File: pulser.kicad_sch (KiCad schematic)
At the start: 15 parts, among them U3 MAX14808ETK_

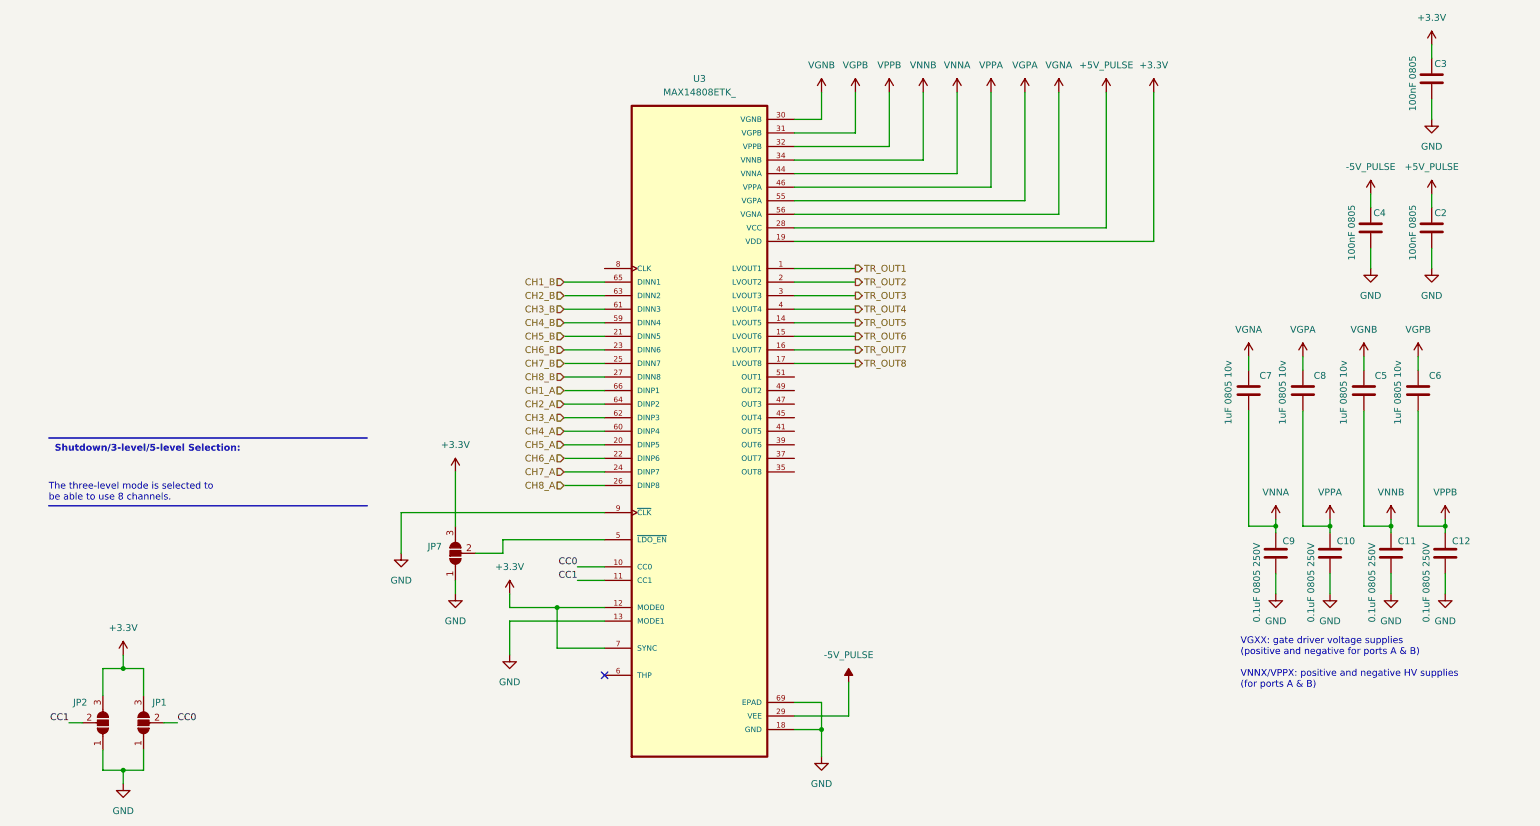
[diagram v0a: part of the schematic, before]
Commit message: finished pulser & mcu, receiver & power remaining
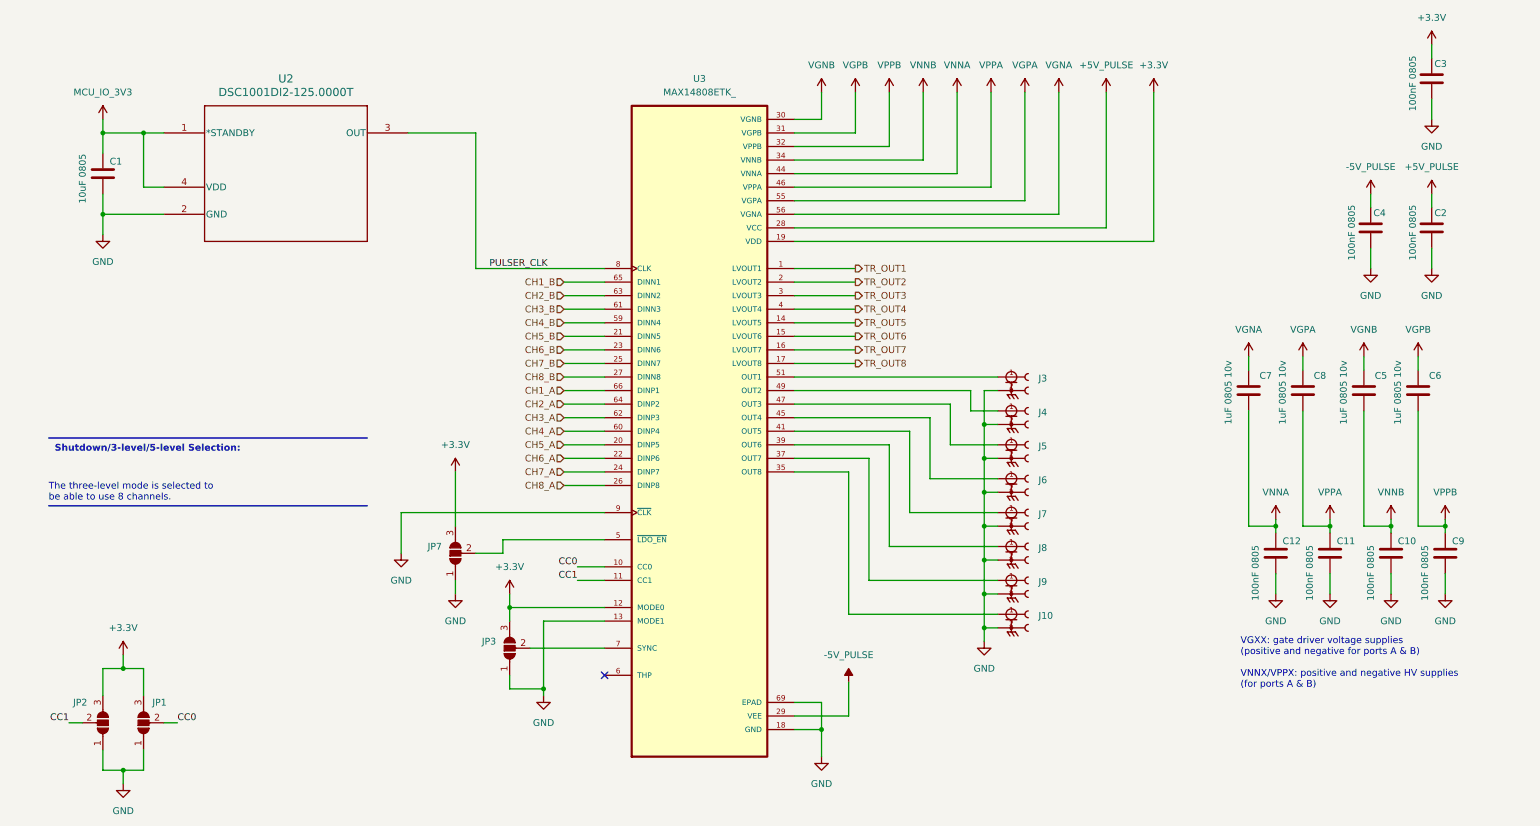
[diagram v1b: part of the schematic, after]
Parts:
- added C1: 10uF 0805, symbol Device:C
- added J10, J3, J4, J5, J6, J7, J8, J9: CONSMA002-SMD, CONSMA002-SMD:TE_CONSMA002-SMD, symbol CONSMA002-SMD:CONSMA002-SMD
- added JP3: SolderJumper_3_Open, symbol Jumper:SolderJumper_3_Open
- added U2: DSC1001DI2-125.0000T, CDFN4_2P5X2_MCH, symbol DSC1001DI2-125.0000T:DSC1001DI2-125.0000T
- C10, C11, C12, C9: value 0.1uF 0805 250V -> 100nF 0805
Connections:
- net +3.3V: now also JP3.3 (B); no longer U3.7 (SYNC)
- net GND: now also C1.2, J10.2, J10.3, J3.2, J3.3, J4.2, J4.3, J5.2, J5.3, J6.2, J6.3, J7.2, J7.3, J8.2, J8.3, J9.2, J9.3, JP3.1 (A), U2.2 (GND)
- net VNNA: now also C12.1; no longer C9.1
- net VNNB: now also C10.1; no longer C11.1
- net VPPA: now also C11.1; no longer C10.1
- net VPPB: now also C9.1; no longer C12.1
- net at U3.35 (OUT8): now also J10.1
- net at U3.37 (OUT7): now also J9.1
- net at U3.39 (OUT6): now also J8.1
- net at U3.41 (OUT5): now also J7.1
- net at U3.45 (OUT4): now also J6.1
- net at U3.47 (OUT3): now also J5.1
- net at U3.49 (OUT2): now also J4.1
- net at U3.51 (OUT1): now also J3.1
- net PULSER_CLK: now reaches U3.8 (CLK)
- net PULSER_CLK: now also U2.3 (OUT)
- new net: JP3.2 (C), U3.7 (SYNC)
- new net MCU_IO_3V3: C1.1, U2.1 (*STANDBY), U2.4 (VDD)

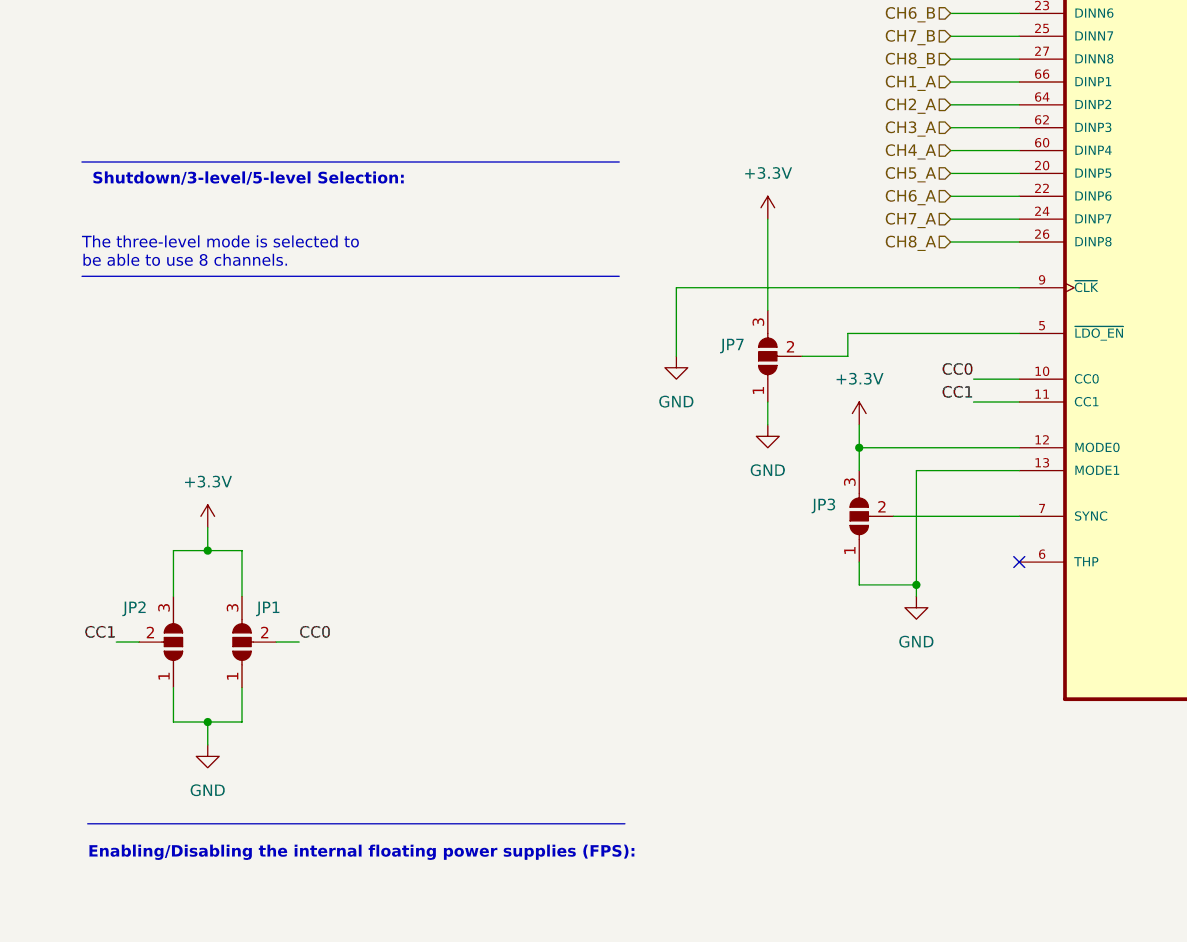
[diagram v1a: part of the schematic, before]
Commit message: converted diff signals to single-ended, modified pulser & MCU, power untouched
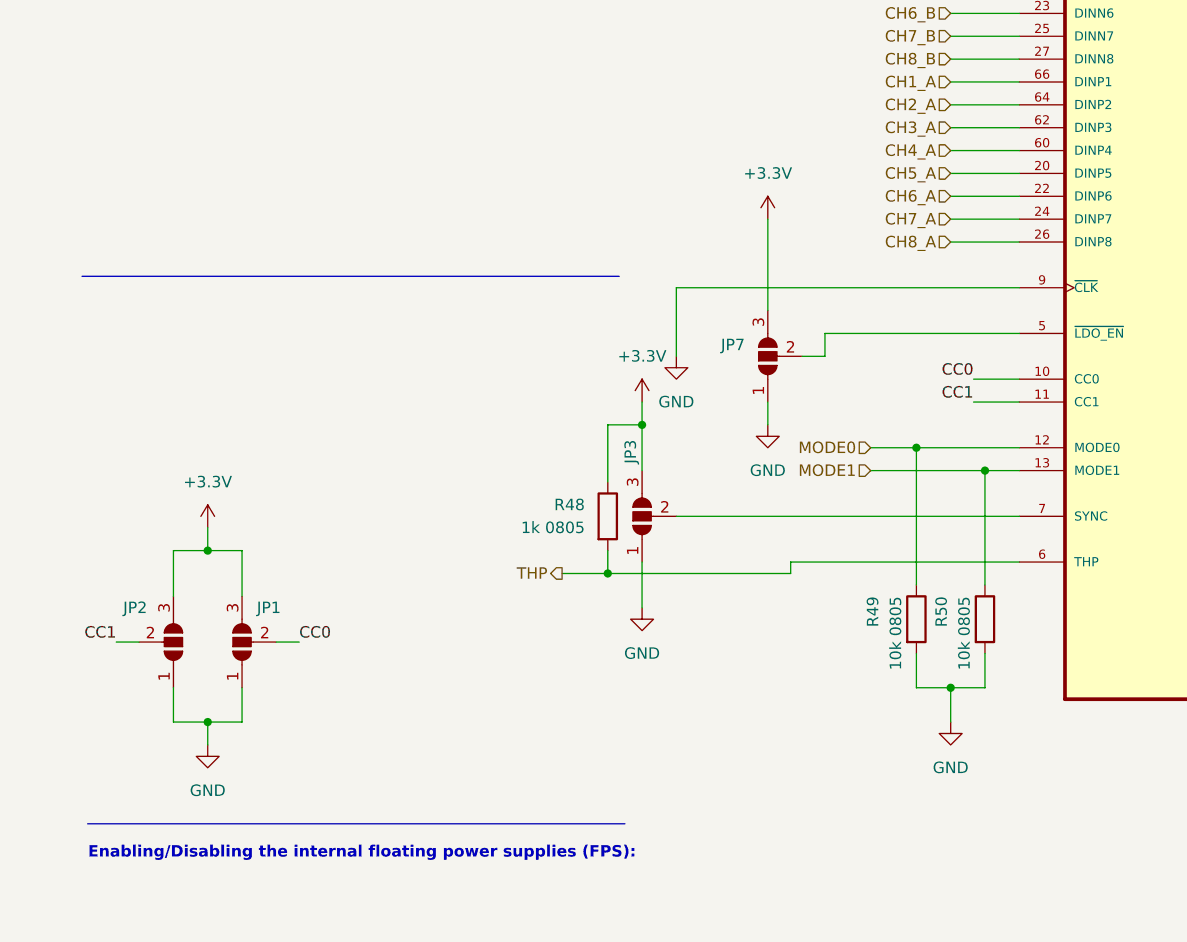
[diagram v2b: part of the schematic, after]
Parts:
- added R48: 1k 0805, symbol Device:R
- added R49, R50: 10k 0805, symbol Device:R
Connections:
- net +3.3V: now also R48.1; no longer U3.12 (MODE0)
- net GND: now also R49.2, R50.2; no longer U3.13 (MODE1)
- net THP: now reaches U3.6 (THP)
- net THP: now also R48.2
- new net MODE0: R49.1, U3.12 (MODE0)
- new net MODE1: R50.1, U3.13 (MODE1)
- no-connect marks 1 -> 0
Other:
- note removed: "Shutdown/3-level/5-level Selection:"
- note removed: "The three-level mode is selected to be able to use 8 channels."
- moved on the sheet: JP3

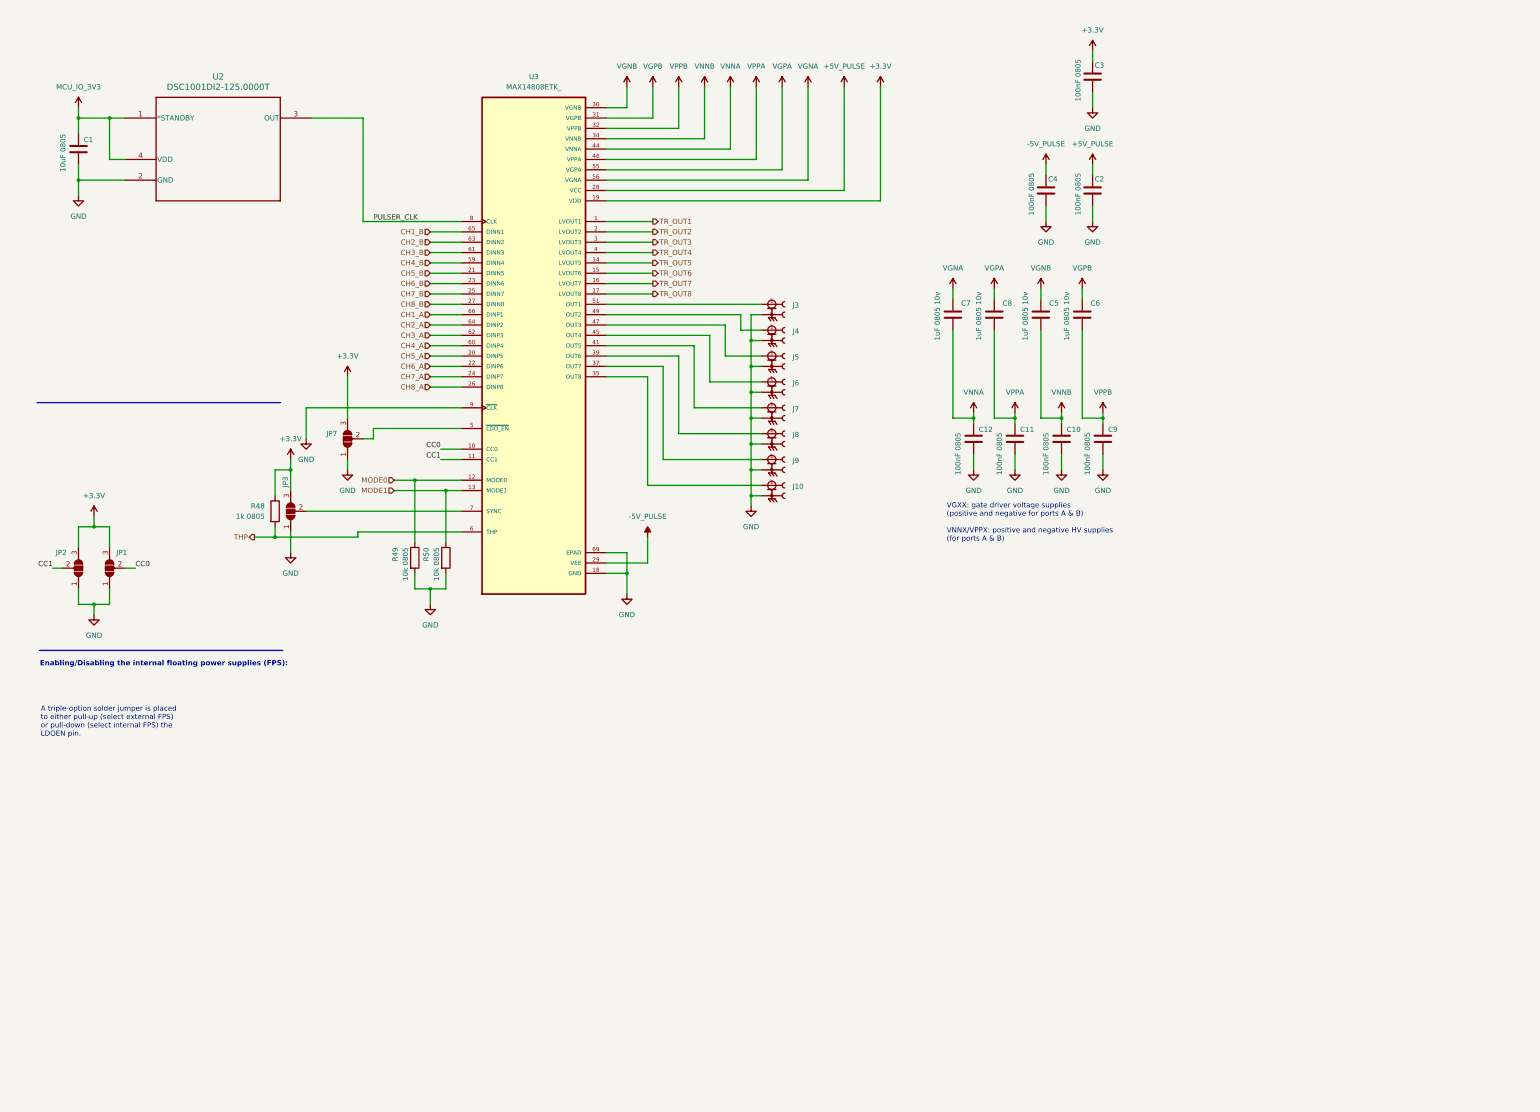
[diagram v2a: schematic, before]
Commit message: finished analog signal chain, added main power components, complete the schematic and form a power budget table
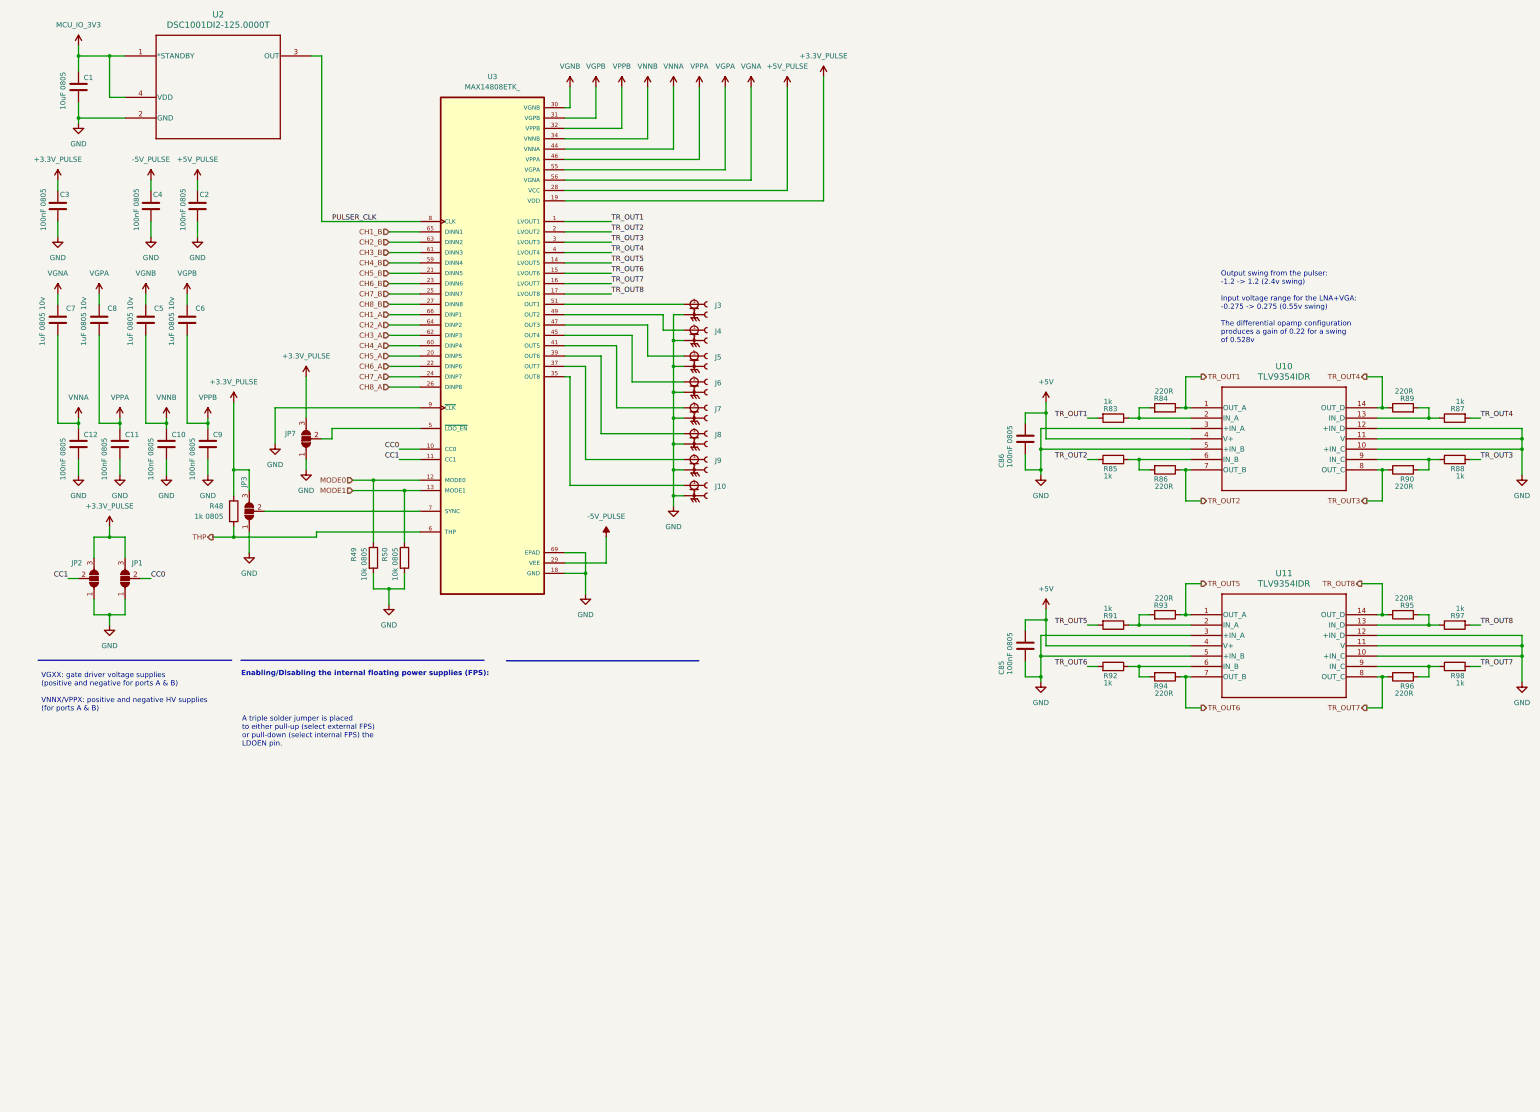
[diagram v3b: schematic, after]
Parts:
- added C85, C86: 100nF 0805, symbol Device:C
- added R83, R85, R87, R88, R91, R92, R97, R98: 1k, symbol Device:R
- added R84, R86, R89, R90, R93, R94, R95, R96: 220R, symbol Device:R
- added U10, U11: TLV9354IDR, SOIC_9354IDR_TEX, symbol 2025-12-09_22-36-51:TLV9354IDR
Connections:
- net GND: now also C85.2, C86.2, U10.10 (+IN_C), U10.11 (V), U10.12 (+IN_D), U10.3 (+IN_A), U10.5 (+IN_B), U11.10 (+IN_C), U11.11 (V), U11.12 (+IN_D), U11.3 (+IN_A), U11.5 (+IN_B)
- net TR_OUT1: now also R83.2, R84.1, U10.1 (OUT_A)
- net TR_OUT2: now also R85.2, R86.1, U10.7 (OUT_B)
- net TR_OUT3: now also R88.2, R90.1, U10.8 (OUT_C)
- net TR_OUT4: now also R87.2, R89.1, U10.14 (OUT_D)
- net TR_OUT5: now also R91.2, R93.1, U11.1 (OUT_A)
- net TR_OUT6: now also R92.2, R94.1, U11.7 (OUT_B)
- net TR_OUT7: now also R96.1, R98.2, U11.8 (OUT_C)
- net TR_OUT8: now also R95.1, R97.2, U11.14 (OUT_D)
- net +3.3V renamed +3.3V_PULSE
- new net: R88.1, R90.2, U10.9 (IN_C)
- new net: R87.1, R89.2, U10.13 (IN_D)
- new net: R95.2, R97.1, U11.13 (IN_D)
- new net: R83.1, R84.2, U10.2 (IN_A)
- new net: R96.2, R98.1, U11.9 (IN_C)
- new net: R85.1, R86.2, U10.6 (IN_B)
- new net: R91.1, R93.2, U11.2 (IN_A)
- new net: R92.1, R94.2, U11.6 (IN_B)
- new net +5V: C85.1, C86.1, U10.4 (V+), U11.4 (V+)
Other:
- note added: "A triple solder jumper is placed to either pull-up (select external FPS) or pull-down (select internal FPS) the LDOEN pin."
- note added: "Output swing from the pulser: -1.2 -> 1.2 (2.4v swing) Input voltage range for the LNA+VGA: -0.275 -> 0.275 (0.55v swing) The differential opamp configuration produces a gain of 0.22 for a swing of 0.528v"
- note removed: "A triple-option solder jumper is placed to either pull-up (select external FPS) or pull-down (select internal FPS) the LDOEN pin."
- moved on the sheet: C1, C10, C11, C12, C2, C3, C4, C5, C6, C7, C8, C9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
